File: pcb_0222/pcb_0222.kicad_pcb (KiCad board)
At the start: 2 copper layers, 80 x 70 mm, 96 parts, among them J1 S2P-VH, J2 SM02B-PASS-TBT, J3 SM02B-PASS-TBT, J4 SM08B-PASS-TBT, J5 TC-2030-IDC, J6 SM08B-PASS-TBT, J7 HEADER_MALE_THT_0.1"_4x1, J8 HEADER_MALE_THT_0.1"_2x1, J9 HEADER_MALE_THT_0.1"_4x1, K1 EE2-3NUH, Q1 BSP170PH6327XTSA1, Q2 BC817-16, U1 LMR54406DBVR, U2 STM32C011F6P6

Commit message: C7, C12 PARTNO upsated + LED4 VALUE updated + S2 MPN changed to CD10RM0SB
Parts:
- LED4: value LTST-C190KSKT -> LTST-C190KRKT
- S2: value 1-1825013-0 -> CD10RM0SB; footprint switches_smd:1-1825013-0 -> switches_smd:CD10RM0SB
- moved R10 7.39 mm to (160.2, 97.9), turned to 90 degrees
- moved R13 7.37 mm to (160.1, 105.9), turned to -90 degrees
- moved TP17 4.80 mm to (158.4, 99.7)
- moved TP9 4.65 mm to (158.4, 104.0)
- moved S2 0.24 mm to (169.1, 102.2), turned to 90 degrees
- moved R12 0.18 mm to (163.4, 97.9)
- moved R11 0.05 mm to (163.5, 105.9)
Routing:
- net /MCU_BCD0: track 48.0 -> 31.7 mm, vias 3 -> 4
- net /MCU_BCD1: track 31.8 -> 39.5 mm
- net /MCU_BCD2: track 31.5 -> 38.8 mm
- net /MCU_BCD3: track 33.7 -> 31.3 mm
- net /MCU_SW1: track 39.1 -> 40.3 mm
- net +3V3: track 41.9 -> 42.7 mm
- net VB: vias 0 -> 7
- net GND: vias 145 -> 153

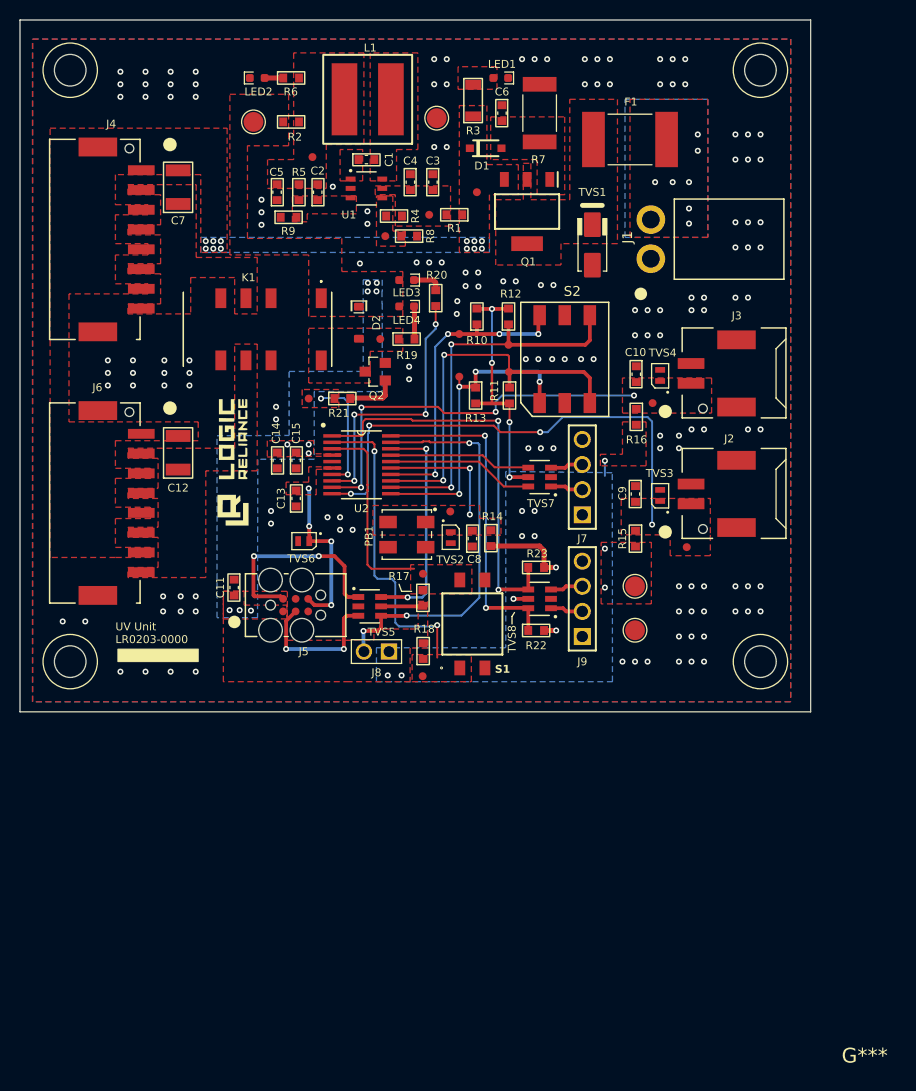
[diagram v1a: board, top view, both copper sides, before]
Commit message: C5, C7, C12 PARTNO and D1, R7 VALUE and PARTNO changed after preliminary layout review
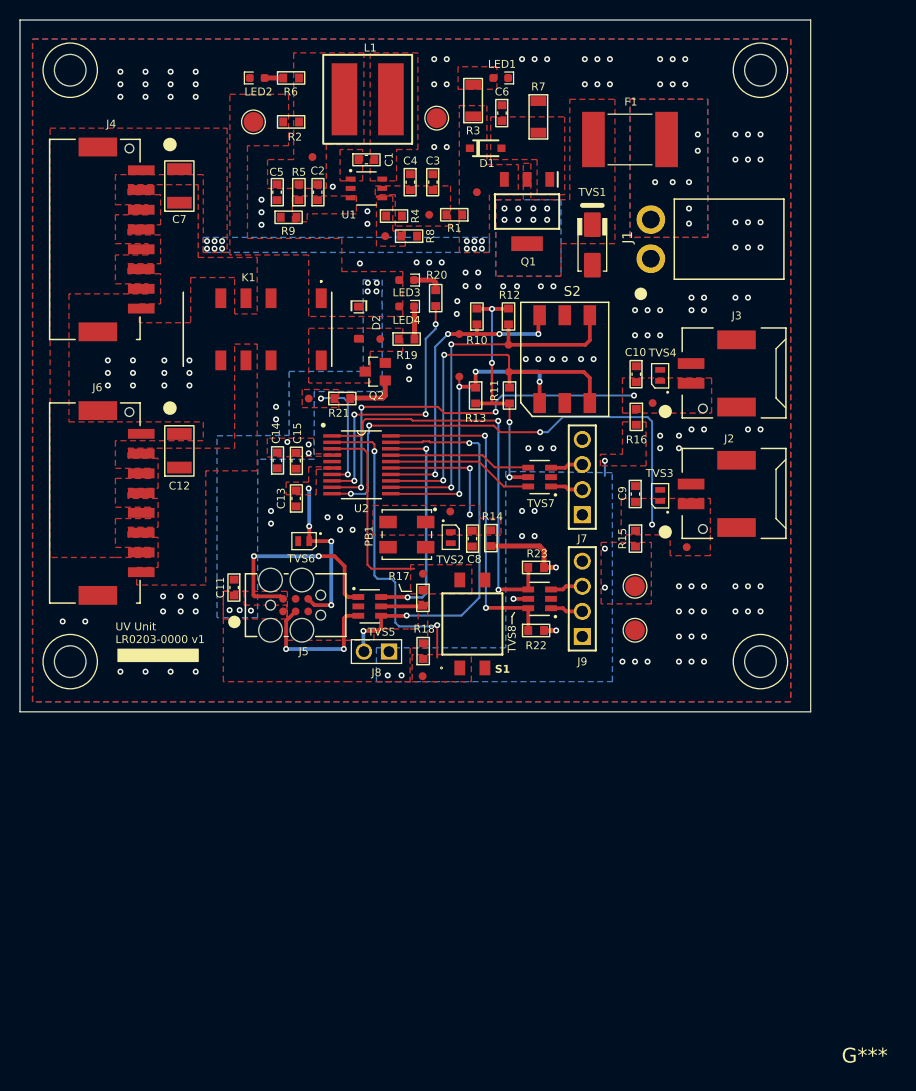
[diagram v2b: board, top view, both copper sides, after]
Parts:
- removed the G*** at (135.6, 111.7)
- D1: value NZH5V1B,115 -> BZT52C5V1
- R7: value 1K -> 3.6K; footprint passives_smd:R_2512 -> passives_smd:R_1206
- moved R7 0.40 mm to (166.4, 77.7)
- moved C12 0.24 mm to (130.1, 111.5)
- moved C7 0.18 mm to (130.1, 84.7)
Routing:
- net Net-(F1-Pad1): vias 0 -> 8
- added copper zone on B.Cu, net Net-(F1-Pad1)
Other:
- board text added: "UV Unit LR0203-0000 v1"
- board text removed: "R7"
- board text removed: "UV Unit LR0203-0000"

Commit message: Layout Review Pass
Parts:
- moved C5 0.20 mm to (140.2, 85.2)
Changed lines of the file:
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@@
 	(title_block
 		(title "UV Floor Sanitization Unit")
-		(date "2026-08-16")
+		(date "2026-08-27")
+		(rev "20260827")
 		(company "Designed by Logic Reliance for Satview Broadband Ltd")
 	)
@@
 		(grid_origin 113.995 137.894)
 		(pcbplotparams
-			(layerselection 0x00000000_00000000_5555555d_55555550)
-			(plot_on_all_layers_selection 0x00000000_00000000_00000008_02000000)
+			(layerselection 0x00000000_00000000_5555555f_5755f5ff)
+			(plot_on_all_layers_selection 0x00000000_00000000_00000000_00000000)
 			(disableapertmacros no)
 			(usegerberextensions no)
@@
 			(mode 1)
 			(useauxorigin no)
-			(pdf_front_fp_property_popups no)
-			(pdf_back_fp_property_popups no)
-			(pdf_metadata no)
+			(pdf_front_fp_property_popups yes)
+			(pdf_back_fp_property_popups yes)
+			(pdf_metadata yes)
 			(pdf_single_document no)
 			(dxfpolygonmode yes)
@@
 			(crossoutdnponfab no)
 			(subtractmaskfromsilk no)
-			(outputformat 4)
+			(outputformat 1)
 			(mirror no)
-			(drillshape 2)
+			(drillshape 0)
 			(scaleselection 1)
-			(outputdirectory "outputs/Manufacture/20260816-P_0222_manufacture/DWG/")
+			(outputdirectory "outputs/Manufacture/20260827-P_0222_manufacture/DRILLS/")
 		)
 	)
@@
 	(footprint "passives_smd:C_0603"
 		(layer "F.Cu")
-		(at 140.0046 85.316 90)
+		(at 140.157 85.189 90)
 		(descr "<b>CAPACITOR</b>")
 		(property "Reference" "C5"
@@
 	)
 	(zone
-		(net "Net-(J9-Pad3)")
-		(layer "F.Cu")
-		(hatch none 0.1)
-		(priority 30000)
-		(attr
-			(teardrop
-				(type padvia)
-			)
-		)
-		(connect_pads yes
-			(clearance 0)
-		)
-		(min_thickness 0.0254)
-		(fill yes
-			(island_removal_mode 1)
-		)
-		(polygon
-			(pts
-				(xy 169.515153 125.0035) (xy 169.515153 125.3845) (xy 170.48442 125.954657) (xy 170.896153 125.194)
-				(xy 170.48442 124.433343)
-			)
-		)
-	)
-	(zone
 		(net "VB_IP")
 		(layer "F.Cu")
@@
 	)
 	(zone
-		(net "/NRST")
-		(layer "F.Cu")
-		(hatch none 0.1)
-		(priority 30004)
-		(attr
-			(teardrop
-				(type padvia)
-			)
-		)
-		(connect_pads yes
-			(clearance 0)
-		)
-		(min_thickness 0.0254)
-		(fill yes
-			(island_removal_mode 1)
-		)
-		(polygon
-			(pts
-				(xy 143.990166 127.2895) (xy 143.990166 126.9085) (xy 143.923904 126.964296) (xy 143.466543 126.224331)
-				(xy 143.151111 126.460911) (xy 142.914531 126.776343) (xy 143.654496 127.233704) (xy 143.7892 127.2895)
-			)
-		)
-	)
-	(zone
 		(net "+3V3")
 		(layer "F.Cu")
@@
 	)
 	(zone
+		(net "Net-(J7-Pad2)")
+		(layer "F.Cu")
+		(hatch none 0.1)
+		(priority 30002)
+		(attr
+			(teardrop
+				(type padvia)
+			)
+		)
+		(connect_pads yes
+			(clearance 0)
+		)
+		(min_thickness 0.0254)
+		(fill yes
+			(island_removal_mode 1)
+		)
+		(polygon
+			(pts
+				(xy 169.515153 115.1991) (xy 169.515153 115.5801) (xy 170.48442 116.175657) (xy 170.896153 115.3896)
+				(xy 170.48442 114.654343)
+			)
+		)
+	)
+	(zone
 		(net "VB_IP")
 		(layer "F.Cu")
@@
 	)
 	(zone
+		(net "Net-(J7-Pad3)")
+		(layer "F.Cu")
+		(hatch none 0.1)
+		(priority 30003)
+		(attr
+			(teardrop
+				(type padvia)
+			)
+		)
+		(connect_pads yes
+			(clearance 0)
+		)
+		(min_thickness 0.0254)
+		(fill yes
+			(island_removal_mode 1)
+		)
+		(polygon
+			(pts
+				(xy 169.515153 112.6845) (xy 169.515153 113.0655) (xy 170.48442 113.635657) (xy 170.896153 112.875)
+				(xy 170.48442 112.114343)
+			)
+		)
+	)
+	(zone
 		(net "GND")
 		(layer "F.Cu")
@@
 	)
 	(zone
-		(net "Net-(J5-SWCLK)")
-		(layer "F.Cu")
-		(hatch none 0.1)
-		(priority 30005)
-		(attr
-			(teardrop
-				(type padvia)
-			)
-		)
-		(connect_pads yes
-			(clearance 0)
-		)
-		(min_thickness 0.0254)
-		(fill yes
-			(island_removal_mode 1)
-		)
-		(polygon
-			(pts
-				(xy 141.195103 128.15369) (xy 141.46451 128.423097) (xy 142.034862 128.097731) (xy 141.887289 127.730911)
-				(xy 141.520469 127.583338)
-			)
-		)
-	)
-	(zone
 		(net "+3V3")
 		(layer "F.Cu")
@@
 	)
 	(zone
-		(net "Net-(J5-SWDIO)")
+		(net "Net-(J9-Pad2)")
 		(layer "F.Cu")
 		(hatch none 0.1)
-		(priority 30006)
+		(priority 30001)
 		(attr
 			(teardrop
@@
 		(polygon
 			(pts
-				(xy 140.079968 126.0195) (xy 140.079968 126.4005) (xy 140.223868 126.48559) (xy 140.710888 126.21)
-				(xy 140.665588 126.073668)
+				(xy 169.515153 127.5435) (xy 169.515153 127.9245) (xy 170.48442 128.494657) (xy 170.896153 127.734)
+				(xy 170.48442 126.973343)
 			)
 		)
@@
 	)
 	(zone
+		(net "Net-(J5-SWCLK)")
+		(layer "F.Cu")
+		(hatch none 0.1)
+		(priority 30005)
+		(attr
+			(teardrop
+				(type padvia)
+			)
+		)
+		(connect_pads yes
+			(clearance 0)
+		)
+		(min_thickness 0.0254)
+		(fill yes
+			(island_removal_mode 1)
+		)
+		(polygon
+			(pts
+				(xy 141.195103 128.15369) (xy 141.46451 128.423097) (xy 142.034862 128.097731) (xy 141.887289 127.730911)
+				(xy 141.520469 127.583338)
+			)
+		)
+	)
+	(zone
 		(net "+3V3")
 		(layer "F.Cu")
@@
 	)
 	(zone
+		(net "Net-(J9-Pad3)")
+		(layer "F.Cu")
+		(hatch none 0.1)
+		(priority 30000)
+		(attr
+			(teardrop
+				(type padvia)
+			)
+		)
+		(connect_pads yes
+			(clearance 0)
+		)
+		(min_thickness 0.0254)
+		(fill yes
+			(island_removal_mode 1)
+		)
+		(polygon
+			(pts
+				(xy 169.515153 125.0035) (xy 169.515153 125.3845) (xy 170.48442 125.954657) (xy 170.896153 125.194)
+				(xy 170.48442 124.433343)
+			)
+		)
+	)
+	(zone
 		(net "Net-(U1-CB)")
 		(layer "F.Cu")
@@
 	)
 	(zone
-		(net "Net-(J9-Pad2)")
-		(layer "F.Cu")
-		(hatch none 0.1)
-		(priority 30001)
-		(attr
-			(teardrop
-				(type padvia)
-			)
-		)
-		(connect_pads yes
-			(clearance 0)
-		)
-		(min_thickness 0.0254)
-		(fill yes
-			(island_removal_mode 1)
-		)
-		(polygon
-			(pts
-				(xy 169.515153 127.5435) (xy 169.515153 127.9245) (xy 170.48442 128.494657) (xy 170.896153 127.734)
-				(xy 170.48442 126.973343)
-			)
-		)
-	)
-	(zone
 		(net "Net-(U1-EN)")
 		(layer "F.Cu")
@@
 	)
 	(zone
-		(net "Net-(J7-Pad2)")
+		(net "Net-(J5-SWDIO)")
 		(layer "F.Cu")
 		(hatch none 0.1)
-		(priority 30002)
+		(priority 30006)
 		(attr
 			(teardrop
@@
 		(polygon
 			(pts
-				(xy 169.515153 115.1991) (xy 169.515153 115.5801) (xy 170.48442 116.175657) (xy 170.896153 115.3896)
-				(xy 170.48442 114.654343)
+				(xy 140.079968 126.0195) (xy 140.079968 126.4005) (xy 140.223868 126.48559) (xy 140.710888 126.21)
+				(xy 140.665588 126.073668)
 			)
 		)
 	)
 	(zone
-		(net "Net-(J7-Pad3)")
+		(net "/NRST")
 		(layer "F.Cu")
 		(hatch none 0.1)
-		(priority 30003)
+		(priority 30004)
 		(attr
 			(teardrop
@@
 		(polygon
 			(pts
-				(xy 169.515153 112.6845) (xy 169.515153 113.0655) (xy 170.48442 113.635657) (xy 170.896153 112.875)
-				(xy 170.48442 112.114343)
+				(xy 143.990166 127.2895) (xy 143.990166 126.9085) (xy 143.923904 126.964296) (xy 143.466543 126.224331)
+				(xy 143.151111 126.460911) (xy 142.914531 126.776343) (xy 143.654496 127.233704) (xy 143.7892 127.2895)
 			)
 		)
@@
 	)
 	(zone
-		(net "/SWCLK")
-		(layer "B.Cu")
-		(hatch none 0.1)
-		(priority 30000)
-		(attr
-			(teardrop
-				(type padvia)
-			)
-		)
-		(connect_pads yes
-			(clearance 0)
-		)
-		(min_thickness 0.0254)
-		(fill yes
-			(island_removal_mode 1)
-		)
-		(polygon
-			(pts
-				(xy 148.9327 130.481973) (xy 148.5517 130.481973) (xy 148.065415 131.409098) (xy 148.7422 131.802973)
-				(xy 149.520585 131.409098)
-			)
-		)
-	)
-	(zone
 		(net "VB")
 		(layer "B.Cu")
@@
 			)
 		)
+	)
+	(zone
+		(net "/SWCLK")
+		(layer "B.Cu")
+		(hatch none 0.1)
+		(priority 30000)
+		(attr
+			(teardrop
+				(type padvia)
+			)
+		)
+		(connect_pads yes
+			(clearance 0)
+		)
+		(min_thickness 0.0254)
+		(fill yes
+			(island_removal_mode 1)
+		)
+		(polygon
+			(pts
+				(xy 148.9327 130.481973) (xy 148.5517 130.481973) (xy 148.065415 131.409098) (xy 148.7422 131.802973)
+				(xy 149.520585 131.409098)
+			)
+		)
